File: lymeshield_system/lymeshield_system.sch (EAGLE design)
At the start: 67 parts, among them J1 TSW-106-16-L-S-RA, J2 M04B, J3 TSW-103-07-G-D-LL, J4 1844210, U1 MCP79410-I_SN, U2 ATMEGA1608-MU, U3 MX25V1635FM1I, U4 OPA2349EA, U5 STSPIN240, U6 DRV5057A2QDBZ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

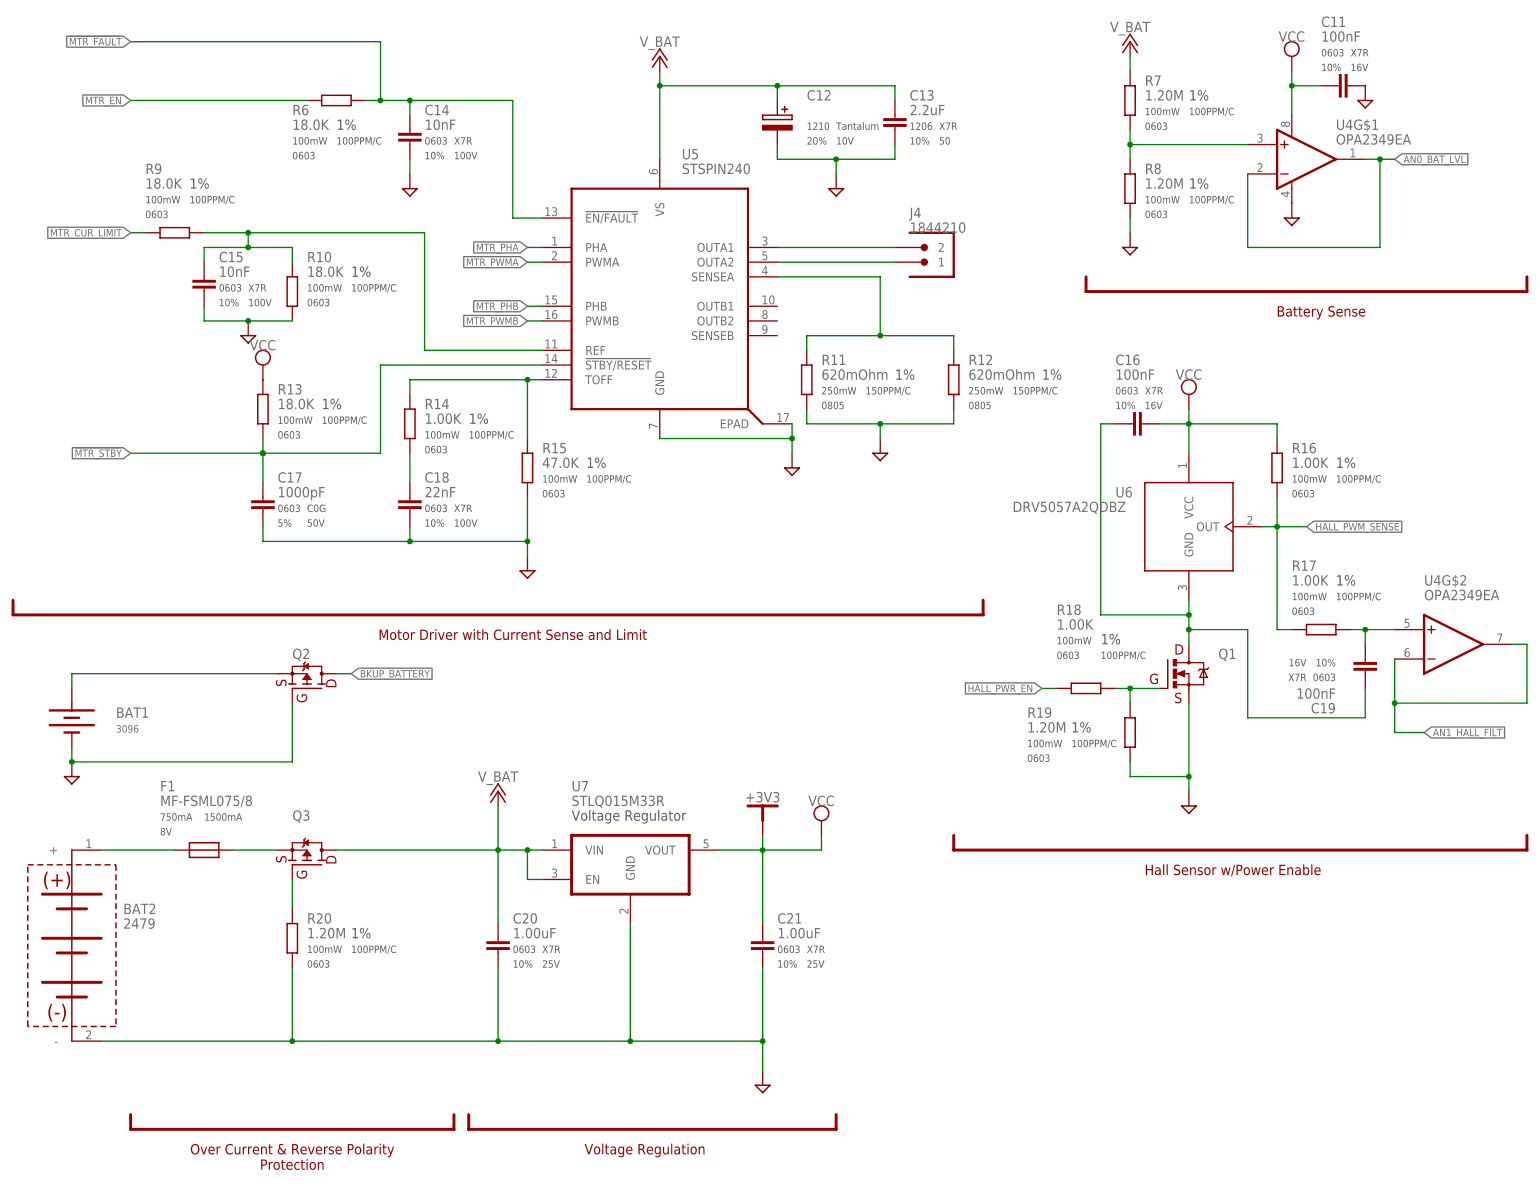
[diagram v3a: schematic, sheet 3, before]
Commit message: fix(lss):  update to R2.2 - Change motor driver
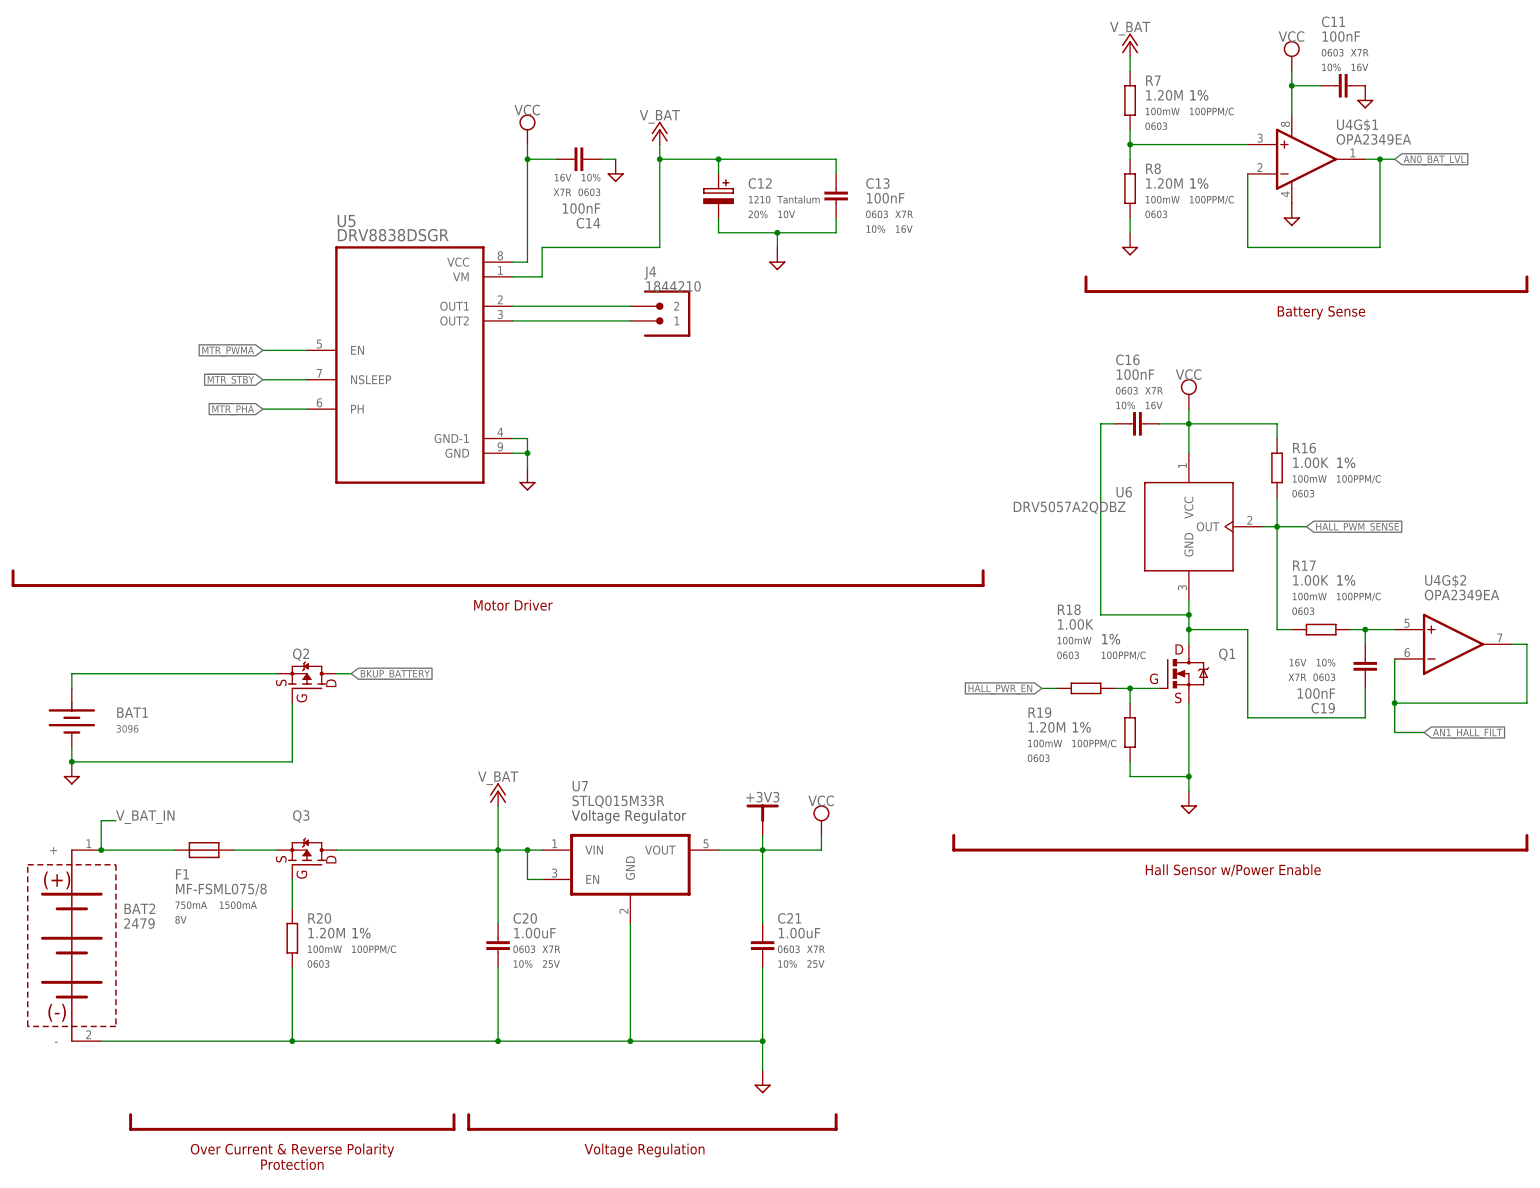
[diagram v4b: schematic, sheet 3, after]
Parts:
- removed C15: 10nF, HatchPoint-Capacitors:GCM188R72A103KA37D
- removed C17: 1000pF, HatchPoint-Capacitors:GCM1885C1H102JA16J
- removed C18: 22nF, HatchPoint-Capacitors:GCM188R72A223KA37D
- removed R10, R13, R6, R9: 18.0K, HatchPoint-Resistors:CRCW060318K0FKEAC
- removed R11, R12: 620mOhm, HatchPoint-Resistors:ERJU6QFR62V
- removed R14: 1.00K, HatchPoint-Resistors:CRCW06031K00FKEAC
- removed R15: 47.0K, HatchPoint-Resistors:CRCW060347K0FKEAC
- C13: value 2.2uF -> 100nF; device HatchPoint-Capacitors:GCM31CR71H225KA55L -> HatchPoint-Capacitors:GCM188R71C104KA37J
- C14: value 10nF -> 100nF; device HatchPoint-Capacitors:GCM188R72A103KA37D -> HatchPoint-Capacitors:GCM188R71C104KA37J
- U5: value STSPIN240 -> DRV8838DSGR; device HatchPoint-TI:STSPIN240 -> HatchPoint-MotionControl:DRV8838DSGR
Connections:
- removed net !MTR_FAULT: C14.1, J3.4, R6.2, U2.PD5, U5.!EN/FAULT
- removed net MTR_CUR_LIMIT: J3.2, R9.1, U2.PC0
- removed net MTR_EN: R6.1, U2.PF2
- removed net MTR_PHB: U5.PHB
- removed net MTR_PWMB: U5.PWMB
- removed net N$11: C18.1, R14.2
- removed net N$15: BAT2.+, F1.1
- removed net N$19: C15.1, R10.1, R9.2, U5.REF
- removed net N$3: R14.1, R15.1, U5.TOFF
- removed net SENSEA: R11.1, R12.1, U5.SENSEA
- new net V_BAT_IN: BAT2.+, F1.1, J1.1, J3.4
- net !MTR_STBY: now also J3.2, U5.NSLEEP; no longer C17.1, R13.2, U5.!STBY/RESET
- net DGND: now also U5.GND-1; no longer C15.2, C17.2, C18.2, R10.2, R11.2, R12.2, R15.2, U5.EPAD
- net MTR_PHA: now also U5.PH; no longer U5.PHA
- net MTR_PWMA: now also U5.EN; no longer U5.PWMA
- net OUTA1: now also U5.OUT1; no longer U5.OUTA1
- net OUTA2: now also U5.OUT2; no longer U5.OUTA2
- net VCC: now also C14.1, U5.VCC; no longer R13.1
- net V_BAT: now also U5.VM; no longer J1.1, U5.VS
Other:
- note added: "- Switch to DVR8838 motordriver. - Modify silkscreen"
- note added: "02/08/22"
- note added: "08/30/22"
- note added: "12/02/21"
- note added: "Motor Driver"
- note added: "R1.4"
- note removed: "02/08/2022"
- note removed: "12/02/2021"
- note removed: "Motor Driver with Current Sense and Limit"
- moved on the sheet: C12, C13, C14, J4

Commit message: fix (schematics/layout): update for 2.3.a build - Add variant "A" to schematics - Modify footprints for polarization - Update silkscreen for 2.3.a
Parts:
- removed C19: 100nF, HatchPoint-Capacitors:GCM188R71C104KA37J
- removed R16: 1.00K, HatchPoint-Resistors:CRCW06031K00FKEAC
- added C15: 100nF, HatchPoint-Capacitors:GCM188R71C104KA37J
- added R6: 1.20M, HatchPoint-Resistors:CRCW06031M20FKEA
- C12: value TAJB226M010RNJ -> 100nF; device HatchPoint-Capacitors:TAJB226M010RNJ -> HatchPoint-Capacitors:GCM188R71C104KA37J; TYPE Tantalum -> (none)
- C13: value 100nF -> TAJB226M010RNJ; device HatchPoint-Capacitors:GCM188R71C104KA37J -> HatchPoint-Capacitors:TAJB226M010RNJ; TYPE (none) -> Tantalum
- R8: value 1.20M -> 1.00K; device HatchPoint-Resistors:CRCW06031M20FKEA -> HatchPoint-Resistors:CRCW06031K00FKEAC
- renumbered C20 to C17, C21 to C18, R17 to R9, R18 to R10, R19 to R11, R20 to R12
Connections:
- net DGND: now also C12.2, C13.-, R7.2; no longer C12.-, C13.2, R8.2
- net HALL_PWM_SENSE: now also R8.2; no longer R16.2
- net N$10: now also R6.2, R7.1; no longer R7.2, R8.1
- net N$20: now also C16.1; no longer C19.1
- net N$23: now also C15.2; no longer C19.2
- net VCC: now also C12.1, C15.1, R8.1; no longer C14.1, C16.1, R16.1
- net V_BAT: now also C13.+, C14.1, R6.1; no longer C12.+, C13.1, R7.1
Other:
- note added: "- Renumber designators - Create Variant A for USB 2022 Build - Library mods for pin1/polarization"
- note added: "09/20/22"
- note added: "R2.1"
- note added: "R2.2"
- note added: "R2.3"
- note removed: "R1.1"
- note removed: "R1.4"
- moved on the sheet: C14, C16, R7, R8
